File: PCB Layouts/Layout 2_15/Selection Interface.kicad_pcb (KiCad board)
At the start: 4 copper layers, 110 x 90 mm, 132 parts, among them P1 CONN_01X02, P11 CONN_01X02, P12 CONN_01X02, P13 CONN_01X10, P14 CONN_01X02, P15 CONN_01X02, P16 CONN_01X02, P18 CONN_02X05, P19 CONN_02X05, P2 CONN_01X02, P21 CONN_02X05, P3 CONN_01X02, P4 CONN_01X02, P5 CONN_01X02, P6 CONN_02X10, P7 CONN_01X02, P8 CONN_02X04, P9 CONN_01X02, U1 CY8C42_(48_TQFP), U2 CY8C42_(48_TQFP), U3 CY8C58_(100_TQFP), U4 CY8C42_(48_TQFP), U5 68_PLCC_Socket_(8468-21B1-RK-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, U6 CY8C42_(48_TQFP), U7 CY8C58_(100_TQFP), U8 USB_2.0_B, U9 USB_2.0_B

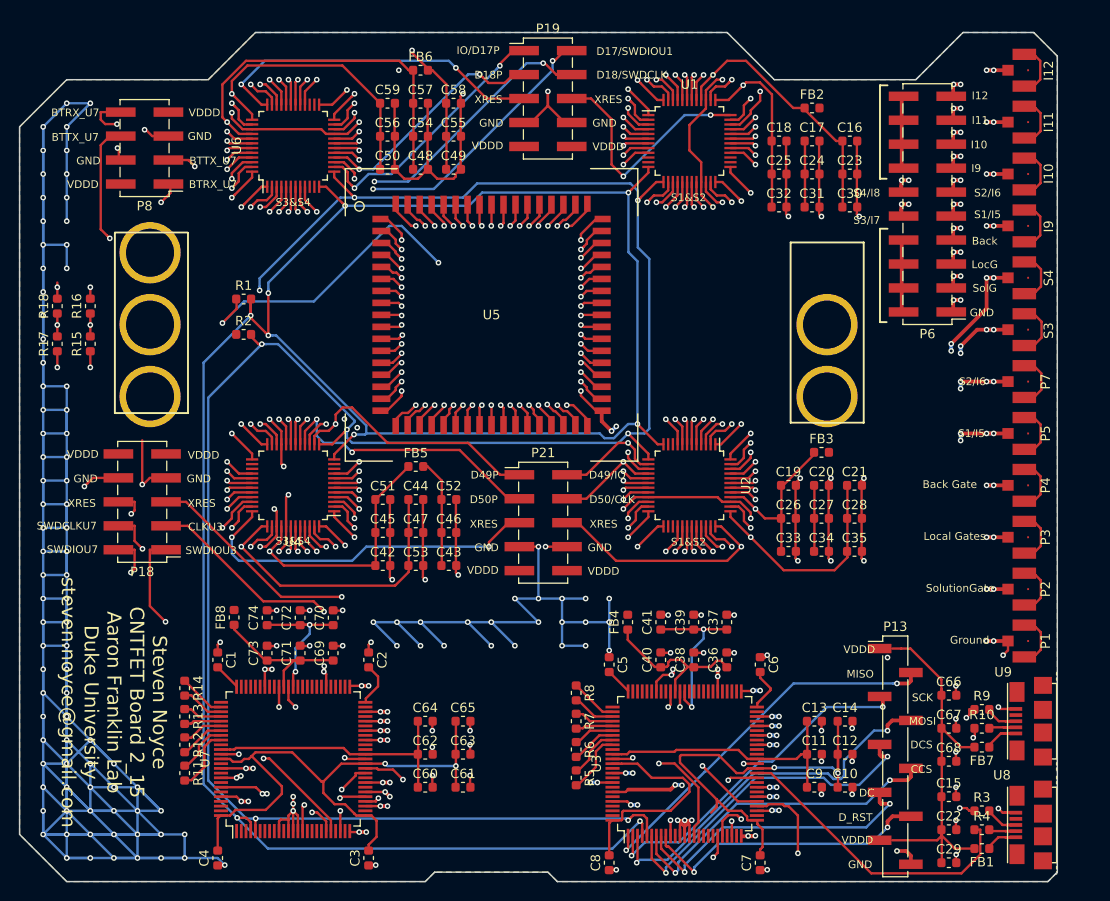
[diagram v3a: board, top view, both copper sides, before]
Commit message: Renamed all of the processors in layout 2_15 so it is much easier to understand
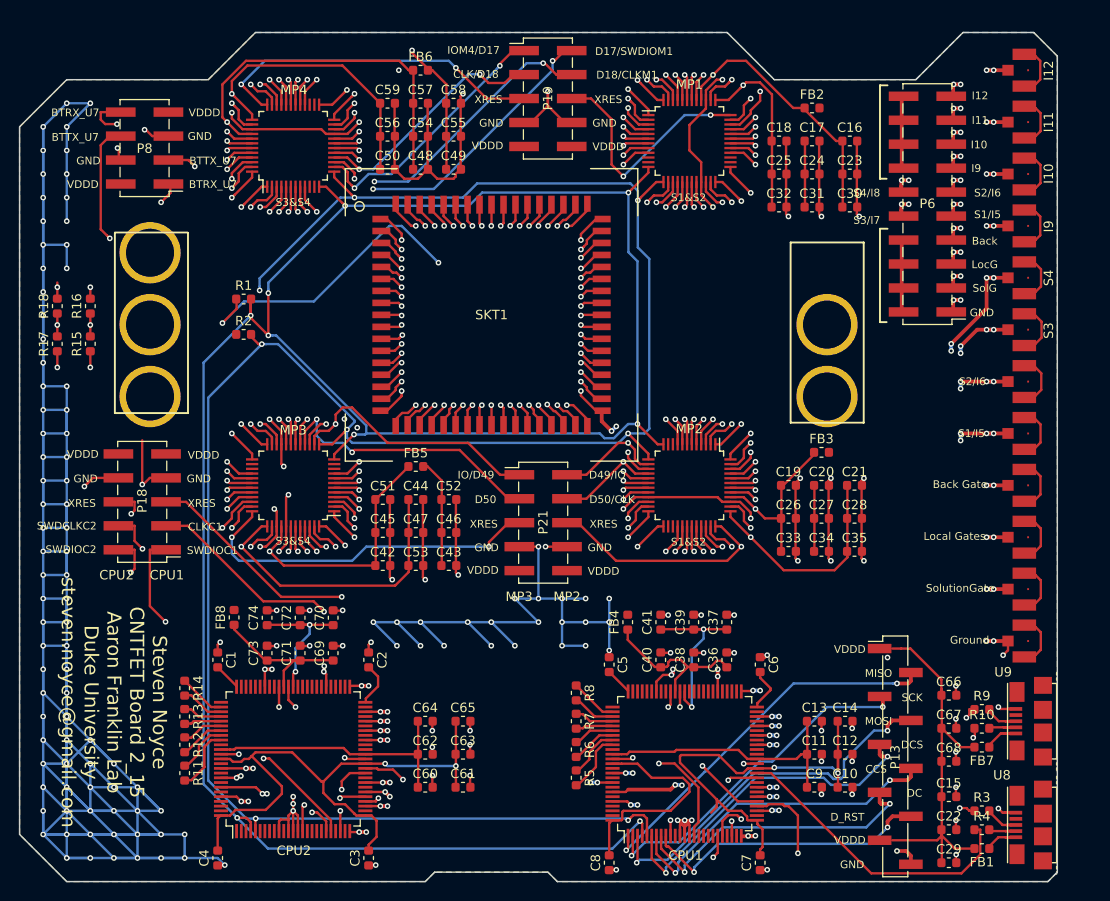
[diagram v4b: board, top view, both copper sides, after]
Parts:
- removed U1, U2, U4, U6: CY8C42_(48_TQFP), Package_QFP:TQFP-48_7x7mm_P0.5mm
- removed U3, U7: CY8C58_(100_TQFP), Package_QFP:TQFP-100_14x14mm_P0.5mm
- removed U5: 68_PLCC_Socket_(8468-21B1-RK-TP), Custom_Footprint_Library:68_PLCC_Socket_(8468-21B1-RK-TP)
- added CPU1: CY8C58_(100_TQFP), Package_QFP:TQFP-100_14x14mm_P0.5mm, F.Cu at (220.5, 147.5)
- added CPU2: CY8C58_(100_TQFP), Package_QFP:TQFP-100_14x14mm_P0.5mm, F.Cu at (179.0, 147.0)
- added MP1: CY8C42_(48_TQFP), Package_QFP:TQFP-48_7x7mm_P0.5mm, F.Cu at (221.0, 81.5)
- added MP2: CY8C42_(48_TQFP), Package_QFP:TQFP-48_7x7mm_P0.5mm, F.Cu at (221.0, 118.0)
- added MP3: CY8C42_(48_TQFP), Package_QFP:TQFP-48_7x7mm_P0.5mm, F.Cu at (179.0, 118.0)
- added MP4: CY8C42_(48_TQFP), Package_QFP:TQFP-48_7x7mm_P0.5mm, F.Cu at (179.0, 82.0)
- added SKT1: 68_PLCC_Socket_(8468-21B1-RK-TP), Custom_Footprint_Library:68_PLCC_Socket_(8468-21B1-RK-TP), F.Cu at (200.0, 99.9)
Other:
- board text added: "CLK/D18"
- board text added: "CLKC1"
- board text added: "CPU1"
- board text added: "CPU2"
- board text added: "D17/SWDIOM1"
- board text added: "D18/CLKM1"
- board text added: "D50"
- board text added: "IO/D49"
- board text added: "IOM4/D17"
- board text added: "MP2"
- board text added: "MP3"
- board text added: "SWDCLKC2"
- board text added: "SWDIOC1"
- board text added: "SWDIOC2"
- board text removed: "CLKU3"
- board text removed: "D17/SWDIOU1"
- board text removed: "D18/SWDCLK"
- board text removed: "D18P"
- board text removed: "D49P"
- board text removed: "D50P"
- board text removed: "IO/D17P"
- board text removed: "SWDCLKU7"
- board text removed: "SWDIOU3"
- board text removed: "SWDIOU7"

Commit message: Continued renaming references and cleaning up layout 2_15
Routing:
- net GND: track 801.3 -> 827.5 mm, vias 201 -> 219
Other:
- board text added: "BTRX_C1"
- board text added: "BTRX_C2"
- board text added: "BTTX_C1"
- board text added: "BTTX_CPU2"
- board text removed: "BTRX_U7"
- board text removed: "BTTX_U7"
- board text removed: "S4/I8"

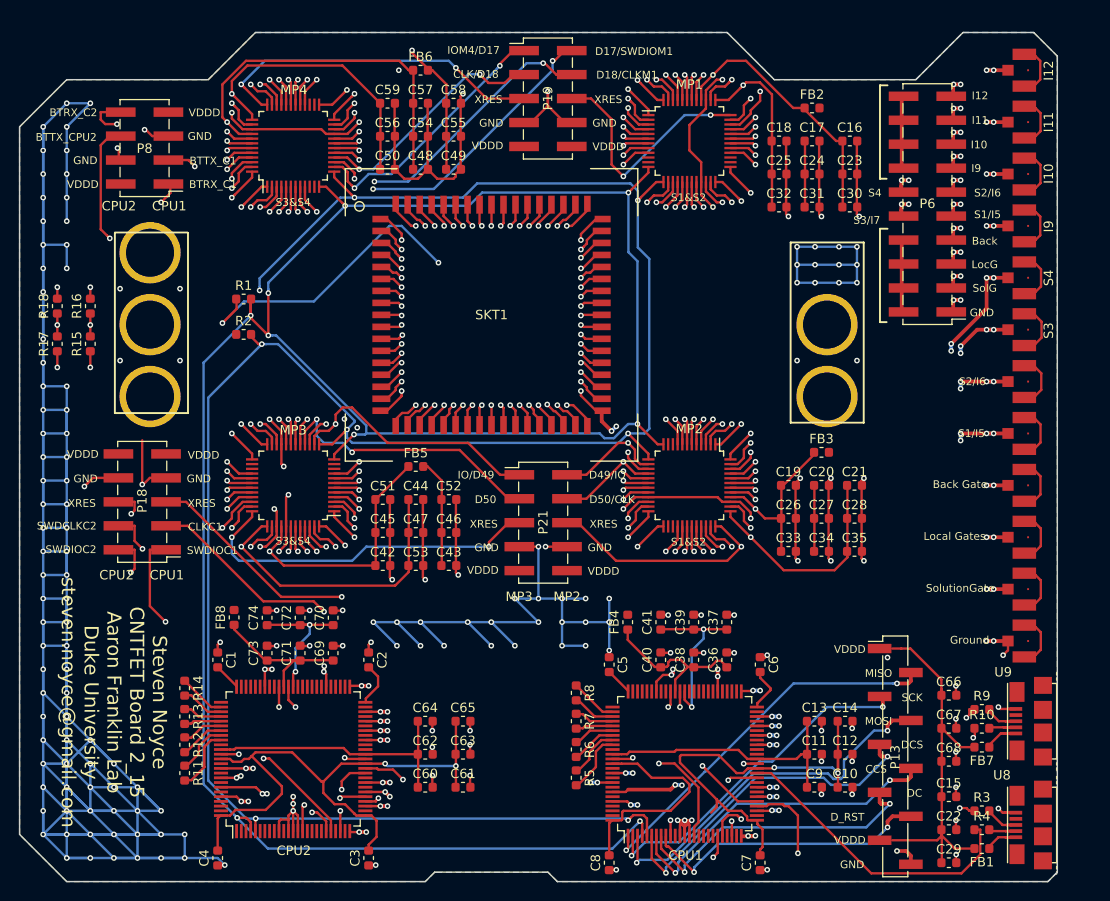
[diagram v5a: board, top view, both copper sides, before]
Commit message: Renamed S1, S2, S3, S4 to SS2, SS1, DD2, DD1 respectively. This is because we have been using S4 and S2 as drain and source in the past. S1 and S3 have been unused but in theory could be used to select another device for simultaneous device measurements
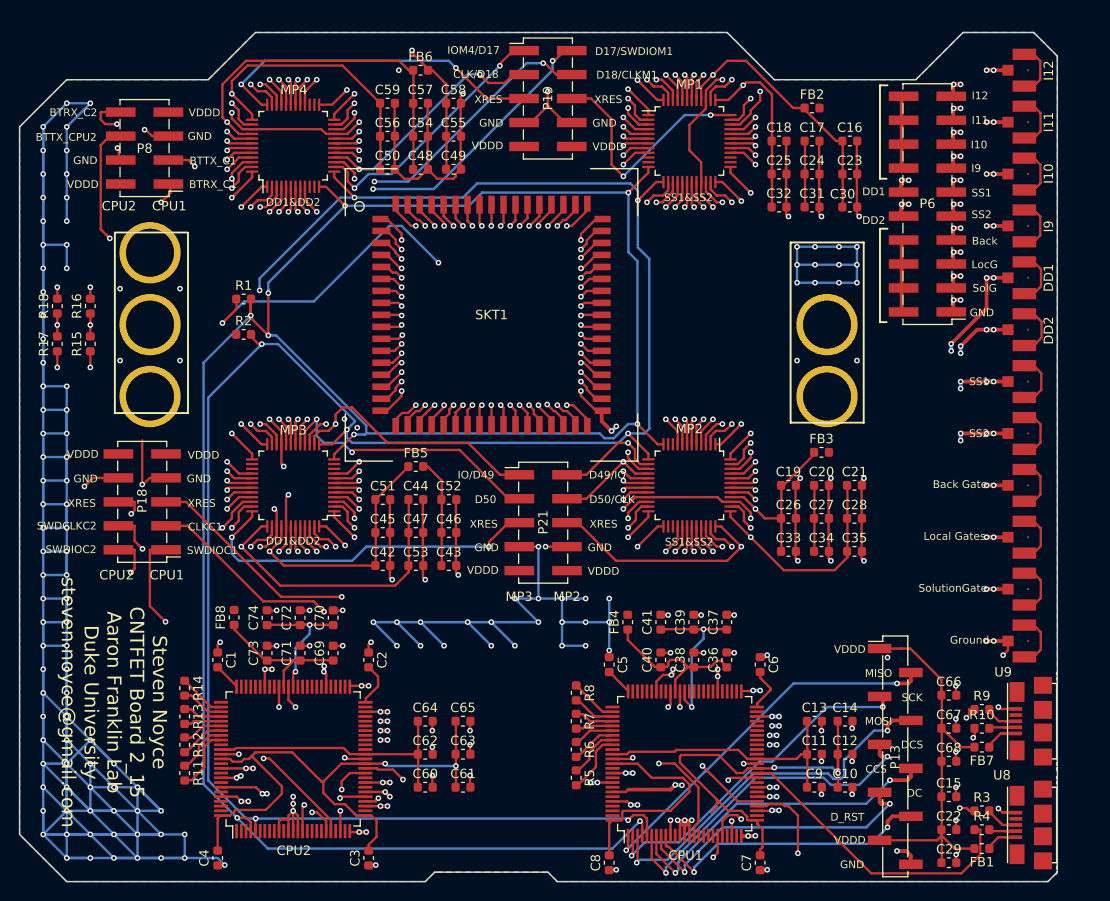
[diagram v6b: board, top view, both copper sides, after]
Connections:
- net I5 renamed SS2
- CPU1 pad 42: I6 -> Net-(CPU1-Pad42)
- CPU1 pad 44: I7 -> Net-(CPU1-Pad44)
- CPU1 pad 46: I8 -> Net-(CPU1-Pad46)
- CPU1 pad 92: I6 -> SS1
- CPU1 pad 94: I7 -> DD2
- CPU1 pad 96: I8 -> DD1
- CPU2 pad 42: I6 -> Net-(CPU2-Pad42)
- CPU2 pad 44: I7 -> Net-(CPU2-Pad44)
- CPU2 pad 46: I8 -> Net-(CPU2-Pad46)
- CPU2 pad 92: I6 -> SS1
- CPU2 pad 94: I7 -> DD2
- CPU2 pad 96: I8 -> DD1
- MP1 pad 34: I6 -> SS1
- MP2 pad 34: I6 -> SS1
- MP3 pad 34: I8 -> DD1
- MP3 pad 35: I7 -> DD2
- MP4 pad 34: I8 -> DD1
- MP4 pad 35: I7 -> DD2
- P11 pad 1: I8 -> DD1
- P6 pad 10: I7 -> DD2
- P6 pad 11: I6 -> SS1
- P6 pad 12: I8 -> DD1
- P7 pad 1: I6 -> SS1
- P9 pad 1: I7 -> DD2
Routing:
- net I7: track 298.9 -> 0.00 mm, vias 16 -> 0
- net DD2: track 0.00 -> 296.0 mm, vias 0 -> 16
- net I8: track 289.8 -> 0.00 mm, vias 16 -> 0
- net DD1: track 0.00 -> 286.7 mm, vias 0 -> 16
- net I6: track 211.7 -> 0.00 mm, vias 16 -> 0
- net SS1: track 0.00 -> 208.9 mm, vias 0 -> 16
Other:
- board text added: "DD1"
- board text added: "DD1&DD2"
- board text added: "DD2"
- board text added: "SS1"
- board text added: "SS1&SS2"
- board text added: "SS2"
- board text removed: "S1&S2"
- board text removed: "S1/I5"
- board text removed: "S2/I6"
- board text removed: "S3"
- board text removed: "S3&S4"
- board text removed: "S3/I7"
- board text removed: "S4"

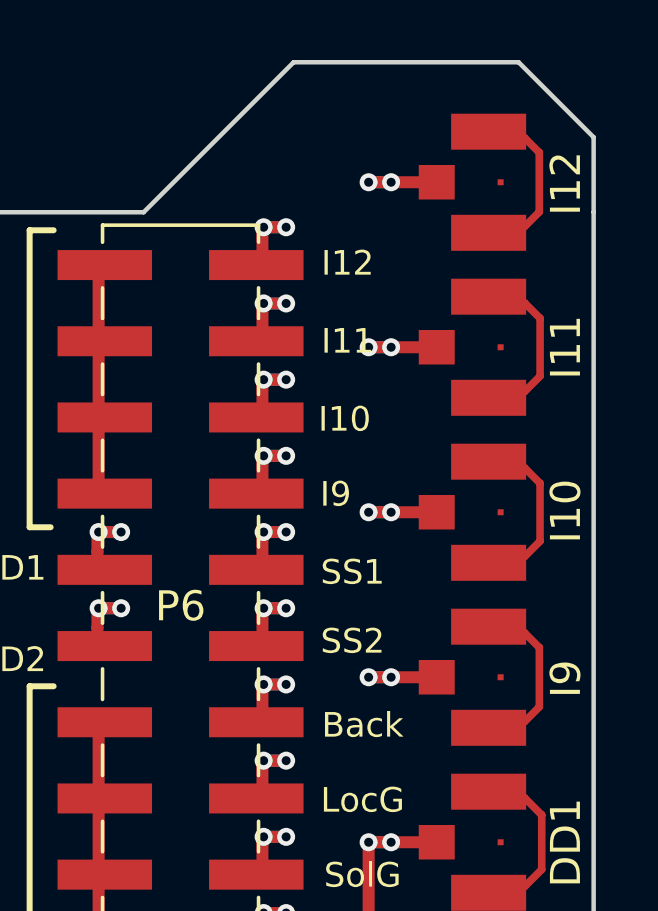
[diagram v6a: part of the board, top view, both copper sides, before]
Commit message: Renamed I9, I10, I11, I12 to IO1, I02, IO3, IO4 respectively. This is because I will likely be moving some of them to different pins on CPU1/CPU2 because we discovered that I9 is currently not functional
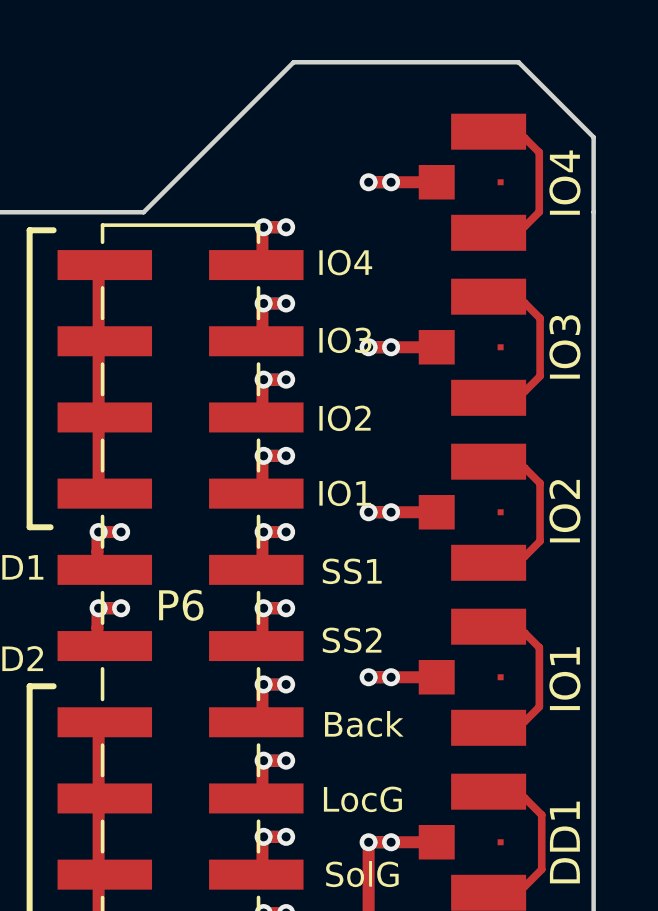
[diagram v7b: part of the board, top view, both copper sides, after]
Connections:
- net I10 renamed IO2
- net I11 renamed IO3
- net I12 renamed IO4
- net I9 renamed IO1
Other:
- board text added: "IO1"
- board text added: "IO2"
- board text added: "IO3"
- board text added: "IO4"
- board text removed: "I10"
- board text removed: "I11"
- board text removed: "I12"
- board text removed: "I9"

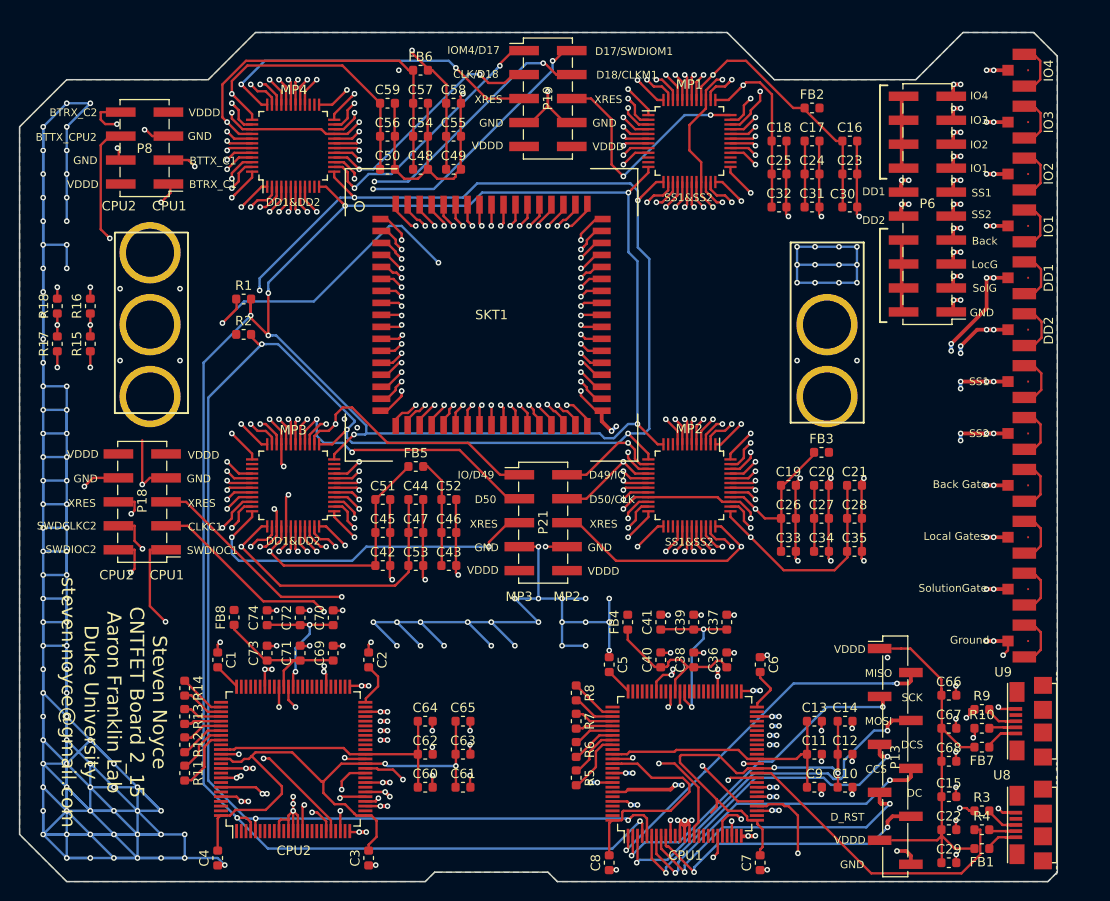
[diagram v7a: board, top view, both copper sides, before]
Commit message: Moved around IO1, IO2, and IO3 so that hopefully all of them will now be attached to functional pins on the cypress chips. Also moved some vias around to satisfy the default design rules checker. This board is in very good shape now and might be worth ordering.
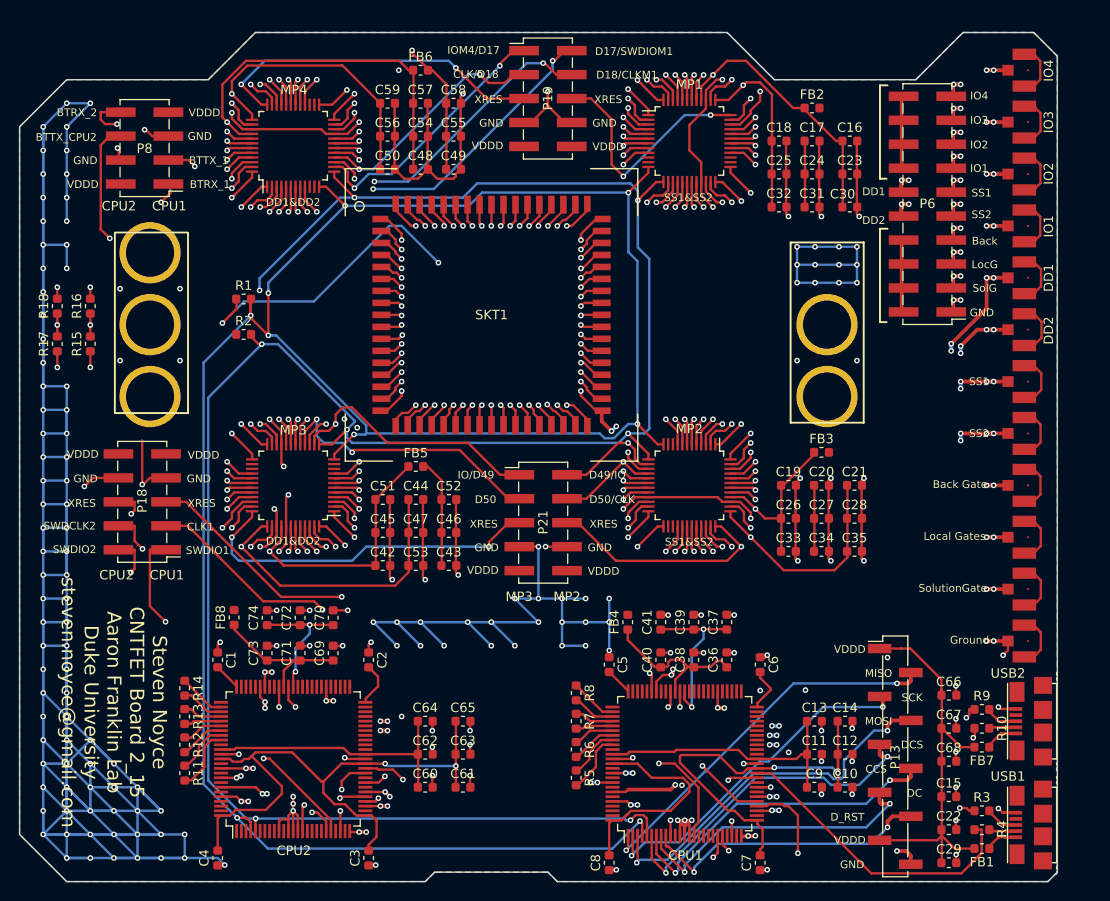
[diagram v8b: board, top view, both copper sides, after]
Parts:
- removed U8, U9: USB_2.0_B, Custom_Footprint_Library:Micro_USB_2.0_B_SMD(10118192-0001LF)
- added USB1: USB_2.0_B, Custom_Footprint_Library:Micro_USB_2.0_B_SMD(10118192-0001LF), F.Cu at (258.5, 154.0)
- added USB2: USB_2.0_B, Custom_Footprint_Library:Micro_USB_2.0_B_SMD(10118192-0001LF), F.Cu at (258.5, 143.0)
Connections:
- net I2 renamed SolutionGate
- net I3 renamed LocalGates
- CPU1 pad 33: SS2 -> IO1
- CPU1 pad 48: IO1 -> Net-(CPU1-Pad48)
- CPU1 pad 51: IO2 -> Net-(CPU1-Pad51)
- CPU1 pad 56: IO3 -> IO2
- CPU1 pad 70: Net-(CPU1-Pad70) -> IO3
- CPU2 pad 33: SS2 -> IO1
- CPU2 pad 48: IO1 -> Net-(CPU2-Pad48)
- CPU2 pad 51: IO2 -> Net-(CPU2-Pad51)
- CPU2 pad 56: IO3 -> IO2
- CPU2 pad 70: Net-(CPU2-Pad70) -> IO3
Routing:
- net IO1: track 130.1 -> 147.3 mm
- net SS2: track 212.2 -> 203.6 mm, vias 16 -> 13
- net IO3: track 134.6 -> 143.1 mm, vias 8 -> 7
- net IO2: track 129.7 -> 136.1 mm, vias 8 -> 9
- net SWDCLK5: track 78.5 -> 75.5 mm
- net Net-(CPU2-Pad36): track 77.4 -> 79.6 mm
- net VDDD: track 319.8 -> 318.3 mm
- net Net-(CPU1-Pad36): track 32.1 -> 33.0 mm
- net SS1: track 208.9 -> 208.1 mm, vias 16 -> 14
- net GND: track 827.5 -> 828.0 mm
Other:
- board text added: "BTRX_1"
- board text added: "BTRX_2"
- board text added: "BTTX_1"
- board text added: "CLK1"
- board text added: "SWDCLK2"
- board text added: "SWDIO1"
- board text added: "SWDIO2"
- board text removed: "BTRX_C1"
- board text removed: "BTRX_C2"
- board text removed: "BTTX_C1"
- board text removed: "CLKC1"
- board text removed: "SWDCLKC2"
- board text removed: "SWDIOC1"
- board text removed: "SWDIOC2"
